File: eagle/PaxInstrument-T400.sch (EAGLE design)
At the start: 133 parts, among them IC1 MCP3424, IC3 SN74LVC1G74DCT, J1 MICRO-SDCARD-CONNECTOR-330006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, Q1 DMP2035U-7, Q2 DMP2035U-7, Q3 DMN2075U-7, Q4 DMN2075U-7, Q5 DMP2035U-7, U1 MCP9800, U2 APX809, U3 MCP73831, U4 MIC5219-3.3V, X1 FH12-12S-1S, Y1 RESONATORSMD

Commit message: Updated SCH and PCB
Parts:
- JP1: value (none) -> ON
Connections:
- removed net DATA1: GND.PF6(ADC6), ICSP1.4, U$3.PF6(ADC6)
- new net RXLED: GND.PB0(SS), U$3.PB0(SS)
- net PWR_ONOFF: now also GND.PF6(ADC6), U$3.PF6(ADC6); no longer GND.PB7, U$3.PB7
- net RTC_INT: now also GND.PB4(ADC11), U$3.PB4(ADC11); no longer GND.PE6, U$3.PE6
- net SW_C: now also GND.PB7, U$3.PB7; no longer GND.PB4(ADC11), U$3.PB4(ADC11)
- net SW_PWR: now also GND.PE6, U$3.PE6; no longer GND.PB0(SS), U$3.PB0(SS)
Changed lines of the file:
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@@
 <part name="GND20" library="SparkFun-Aesthetics" deviceset="GND" device=""/>
 <part name="P+8" library="SparkFun" deviceset="3.3V" device=""/>
-<part name="JP1" library="SparkFun-Passives" deviceset="JUMPER-2" device="SMD-NO">
+<part name="JP1" library="SparkFun-Passives" deviceset="JUMPER-2" device="SMD-NO" value="ON">
 <attribute name="MF" value="N/A"/>
 <attribute name="MPN" value="N/A"/>
@@
 </segment>
 <segment>
-<wire x1="81.28" y1="124.46" x2="83.82" y2="124.46" width="0.1524" layer="91"/>
-<label x="83.82" y="124.46" size="1.778" layer="95"/>
-<pinref part="GND" gate="G$1" pin="PB7"/>
-<pinref part="U$3" gate="G$1" pin="PB7"/>
-<junction x="81.28" y="124.46"/>
+<wire x1="81.28" y1="172.72" x2="83.82" y2="172.72" width="0.1524" layer="91"/>
+<label x="83.82" y="172.72" size="1.778" layer="95"/>
+<pinref part="GND" gate="G$1" pin="PF6(ADC6)"/>
+<pinref part="U$3" gate="G$1" pin="PF6(ADC6)"/>
+<junction x="81.28" y="172.72"/>
 </segment>
 </net>
@@
 </segment>
 <segment>
-<wire x1="81.28" y1="132.08" x2="83.82" y2="132.08" width="0.1524" layer="91"/>
-<label x="83.82" y="132.08" size="1.778" layer="95"/>
-<pinref part="GND" gate="G$1" pin="PB4(ADC11)"/>
-<pinref part="U$3" gate="G$1" pin="PB4(ADC11)"/>
-<junction x="81.28" y="132.08"/>
+<wire x1="81.28" y1="124.46" x2="83.82" y2="124.46" width="0.1524" layer="91"/>
+<label x="83.82" y="124.46" size="1.778" layer="95"/>
+<pinref part="GND" gate="G$1" pin="PB7"/>
+<pinref part="U$3" gate="G$1" pin="PB7"/>
+<junction x="81.28" y="124.46"/>
 </segment>
 </net>
@@
 </segment>
 <segment>
-<wire x1="81.28" y1="116.84" x2="83.82" y2="116.84" width="0.1524" layer="91"/>
-<label x="83.82" y="116.84" size="1.778" layer="95"/>
-<pinref part="GND" gate="G$1" pin="PB0(SS)"/>
-<pinref part="U$3" gate="G$1" pin="PB0(SS)"/>
-<junction x="81.28" y="116.84"/>
+<wire x1="81.28" y1="134.62" x2="83.82" y2="134.62" width="0.1524" layer="91"/>
+<label x="83.82" y="134.62" size="1.778" layer="95"/>
+<pinref part="GND" gate="G$1" pin="PE6"/>
+<pinref part="U$3" gate="G$1" pin="PE6"/>
+<junction x="81.28" y="134.62"/>
 </segment>
 </net>
@@
 </segment>
 <segment>
-<wire x1="81.28" y1="134.62" x2="83.82" y2="134.62" width="0.1524" layer="91"/>
-<label x="83.82" y="134.62" size="1.778" layer="95"/>
-<pinref part="GND" gate="G$1" pin="PE6"/>
-<pinref part="U$3" gate="G$1" pin="PE6"/>
-<junction x="81.28" y="134.62"/>
+<wire x1="81.28" y1="132.08" x2="83.82" y2="132.08" width="0.1524" layer="91"/>
+<label x="83.82" y="132.08" size="1.778" layer="95"/>
+<pinref part="GND" gate="G$1" pin="PB4(ADC11)"/>
+<pinref part="U$3" gate="G$1" pin="PB4(ADC11)"/>
+<junction x="81.28" y="132.08"/>
 </segment>
 </net>
@@
 </segment>
 </net>
-<net name="TXLED" class="0">
-<segment>
-<wire x1="81.28" y1="104.14" x2="83.82" y2="104.14" width="0.1524" layer="91"/>
-<label x="83.82" y="104.14" size="1.778" layer="95"/>
-<pinref part="GND" gate="G$1" pin="PD5"/>
-<pinref part="U$3" gate="G$1" pin="PD5"/>
-<junction x="81.28" y="104.14"/>
-</segment>
-</net>
 <net name="N$10" class="0">
 <segment>
@@
 <pinref part="U$3" gate="G$1" pin="AREF"/>
 <junction x="45.72" y="162.56"/>
-</segment>
-</net>
-<net name="DATA1" class="0">
-<segment>
-<wire x1="81.28" y1="172.72" x2="83.82" y2="172.72" width="0.1524" layer="91"/>
-<label x="83.82" y="172.72" size="1.778" layer="95"/>
-<pinref part="GND" gate="G$1" pin="PF6(ADC6)"/>
-<pinref part="U$3" gate="G$1" pin="PF6(ADC6)"/>
-<junction x="81.28" y="172.72"/>
-</segment>
-<segment>
-<label x="294.64" y="93.98" size="1.778" layer="95"/>
-<pinref part="ICSP1" gate="G$1" pin="4"/>
-<wire x1="294.64" y1="93.98" x2="292.1" y2="93.98" width="0.1524" layer="91"/>
 </segment>
 </net>
@@
 </segment>
 </net>
+<net name="RXLED" class="0">
+<segment>
+<wire x1="81.28" y1="116.84" x2="83.82" y2="116.84" width="0.1524" layer="91"/>
+<label x="83.82" y="116.84" size="1.778" layer="95"/>
+<pinref part="GND" gate="G$1" pin="PB0(SS)"/>
+<pinref part="U$3" gate="G$1" pin="PB0(SS)"/>
+<junction x="81.28" y="116.84"/>
+</segment>
+</net>
+<net name="TXLED" class="0">
+<segment>
+<wire x1="81.28" y1="104.14" x2="83.82" y2="104.14" width="0.1524" layer="91"/>
+<label x="83.82" y="104.14" size="1.778" layer="95"/>
+<pinref part="GND" gate="G$1" pin="PD5"/>
+<pinref part="U$3" gate="G$1" pin="PD5"/>
+<junction x="81.28" y="104.14"/>
+</segment>
+</net>

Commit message: Updated PCB layout
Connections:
- removed net TXLED: GND.PD5, U$3.PD5
- new net DATA1: GND.PF6(ADC6), ICSP1.4, U$3.PF6(ADC6)
- net PWR_ONOFF: now also GND.PD5, U$3.PD5; no longer GND.PF6(ADC6), U$3.PF6(ADC6)
- net RTC_INT: now also GND.PD2(RX), U$3.PD2(RX); no longer GND.PB4(ADC11), U$3.PB4(ADC11)
- net SW_A: now also GND.PE6, U$3.PE6; no longer GND.PD3(TX), U$3.PD3(TX)
- net SW_B: now also GND.PD3(TX), U$3.PD3(TX); no longer GND.PD2(RX), U$3.PD2(RX)
- net SW_C: now also GND.PB4(ADC11), U$3.PB4(ADC11); no longer GND.PB7, U$3.PB7
- net SW_PWR: now also GND.PB7, U$3.PB7; no longer GND.PE6, U$3.PE6
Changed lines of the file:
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@@
 </segment>
 <segment>
-<wire x1="81.28" y1="172.72" x2="83.82" y2="172.72" width="0.1524" layer="91"/>
-<label x="83.82" y="172.72" size="1.778" layer="95"/>
-<pinref part="GND" gate="G$1" pin="PF6(ADC6)"/>
-<pinref part="U$3" gate="G$1" pin="PF6(ADC6)"/>
-<junction x="81.28" y="172.72"/>
+<wire x1="81.28" y1="104.14" x2="83.82" y2="104.14" width="0.1524" layer="91"/>
+<label x="83.82" y="104.14" size="1.778" layer="95"/>
+<pinref part="GND" gate="G$1" pin="PD5"/>
+<pinref part="U$3" gate="G$1" pin="PD5"/>
+<junction x="81.28" y="104.14"/>
 </segment>
 </net>
@@
 </segment>
 <segment>
-<wire x1="81.28" y1="152.4" x2="83.82" y2="152.4" width="0.1524" layer="91"/>
-<label x="83.82" y="152.4" size="1.778" layer="95"/>
-<pinref part="GND" gate="G$1" pin="PD2(RX)"/>
-<pinref part="U$3" gate="G$1" pin="PD2(RX)"/>
-<junction x="81.28" y="152.4"/>
+<wire x1="81.28" y1="149.86" x2="83.82" y2="149.86" width="0.1524" layer="91"/>
+<label x="83.82" y="149.86" size="1.778" layer="95"/>
+<pinref part="GND" gate="G$1" pin="PD3(TX)"/>
+<pinref part="U$3" gate="G$1" pin="PD3(TX)"/>
+<junction x="81.28" y="149.86"/>
 </segment>
 </net>
@@
 </segment>
 <segment>
-<wire x1="81.28" y1="124.46" x2="83.82" y2="124.46" width="0.1524" layer="91"/>
-<label x="83.82" y="124.46" size="1.778" layer="95"/>
-<pinref part="GND" gate="G$1" pin="PB7"/>
-<pinref part="U$3" gate="G$1" pin="PB7"/>
-<junction x="81.28" y="124.46"/>
+<wire x1="81.28" y1="132.08" x2="83.82" y2="132.08" width="0.1524" layer="91"/>
+<label x="83.82" y="132.08" size="1.778" layer="95"/>
+<pinref part="GND" gate="G$1" pin="PB4(ADC11)"/>
+<pinref part="U$3" gate="G$1" pin="PB4(ADC11)"/>
+<junction x="81.28" y="132.08"/>
 </segment>
 </net>
@@
 </segment>
 <segment>
-<wire x1="81.28" y1="149.86" x2="83.82" y2="149.86" width="0.1524" layer="91"/>
-<label x="83.82" y="149.86" size="1.778" layer="95"/>
-<pinref part="GND" gate="G$1" pin="PD3(TX)"/>
-<pinref part="U$3" gate="G$1" pin="PD3(TX)"/>
-<junction x="81.28" y="149.86"/>
+<wire x1="81.28" y1="134.62" x2="83.82" y2="134.62" width="0.1524" layer="91"/>
+<label x="83.82" y="134.62" size="1.778" layer="95"/>
+<pinref part="GND" gate="G$1" pin="PE6"/>
+<pinref part="U$3" gate="G$1" pin="PE6"/>
+<junction x="81.28" y="134.62"/>
 </segment>
 </net>
@@
 </segment>
 <segment>
-<wire x1="81.28" y1="134.62" x2="83.82" y2="134.62" width="0.1524" layer="91"/>
-<label x="83.82" y="134.62" size="1.778" layer="95"/>
-<pinref part="GND" gate="G$1" pin="PE6"/>
-<pinref part="U$3" gate="G$1" pin="PE6"/>
-<junction x="81.28" y="134.62"/>
+<wire x1="81.28" y1="124.46" x2="83.82" y2="124.46" width="0.1524" layer="91"/>
+<label x="83.82" y="124.46" size="1.778" layer="95"/>
+<pinref part="GND" gate="G$1" pin="PB7"/>
+<pinref part="U$3" gate="G$1" pin="PB7"/>
+<junction x="81.28" y="124.46"/>
 </segment>
 </net>
@@
 </segment>
 <segment>
-<wire x1="81.28" y1="132.08" x2="83.82" y2="132.08" width="0.1524" layer="91"/>
-<label x="83.82" y="132.08" size="1.778" layer="95"/>
-<pinref part="GND" gate="G$1" pin="PB4(ADC11)"/>
-<pinref part="U$3" gate="G$1" pin="PB4(ADC11)"/>
-<junction x="81.28" y="132.08"/>
+<wire x1="81.28" y1="152.4" x2="83.82" y2="152.4" width="0.1524" layer="91"/>
+<label x="83.82" y="152.4" size="1.778" layer="95"/>
+<pinref part="GND" gate="G$1" pin="PD2(RX)"/>
+<pinref part="U$3" gate="G$1" pin="PD2(RX)"/>
+<junction x="81.28" y="152.4"/>
 </segment>
 </net>
@@
 </segment>
 </net>
-<net name="TXLED" class="0">
-<segment>
-<wire x1="81.28" y1="104.14" x2="83.82" y2="104.14" width="0.1524" layer="91"/>
-<label x="83.82" y="104.14" size="1.778" layer="95"/>
-<pinref part="GND" gate="G$1" pin="PD5"/>
-<pinref part="U$3" gate="G$1" pin="PD5"/>
-<junction x="81.28" y="104.14"/>
-</segment>
-</net>
+<net name="DATA1" class="0">
+<segment>
+<wire x1="81.28" y1="172.72" x2="83.82" y2="172.72" width="0.1524" layer="91"/>
+<label x="83.82" y="172.72" size="1.778" layer="95"/>
+<pinref part="GND" gate="G$1" pin="PF6(ADC6)"/>
+<pinref part="U$3" gate="G$1" pin="PF6(ADC6)"/>
+<junction x="81.28" y="172.72"/>
+</segment>
+<segment>
+<pinref part="ICSP1" gate="G$1" pin="4"/>
+<wire x1="292.1" y1="93.98" x2="294.64" y2="93.98" width="0.1524" layer="91"/>
+<label x="294.64" y="93.98" size="1.778" layer="95"/>
+</segment>
+</net>

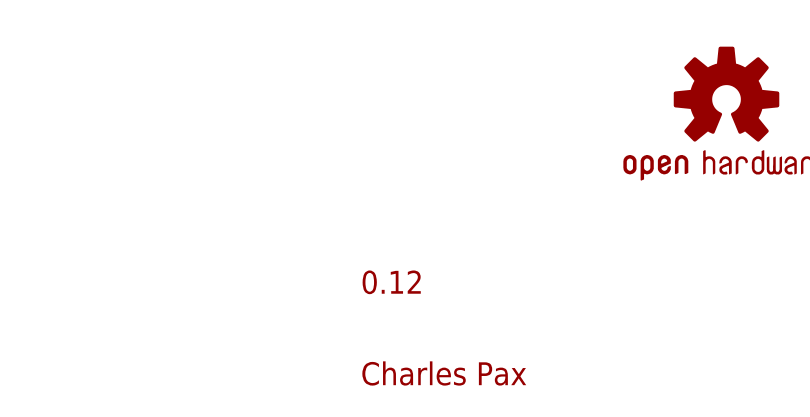
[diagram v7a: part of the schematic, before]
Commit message: Updated Schematic
updated version number on schematic
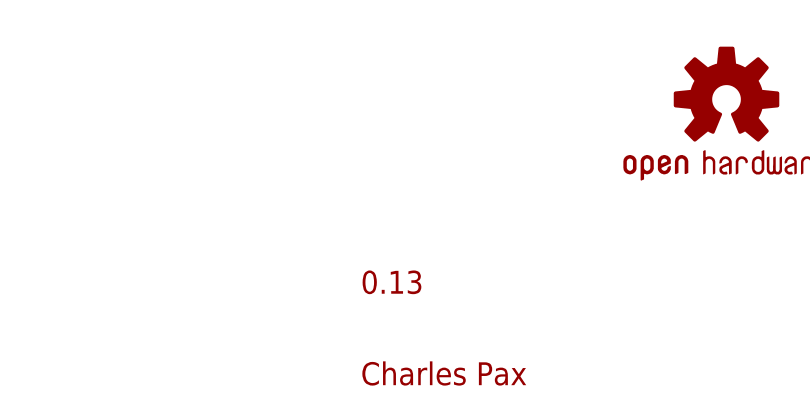
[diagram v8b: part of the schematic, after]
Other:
- note added: "0.13"
- note removed: "0.12"
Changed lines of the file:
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@@
 <wire x1="195.58" y1="154.94" x2="195.58" y2="193.04" width="0.2032" layer="94"/>
 <text x="198.12" y="187.96" size="3.81" layer="94">Temp sensor</text>
-<text x="330.2" y="15.24" size="2.54" layer="94" align="center-left">0.12</text>
+<text x="330.2" y="15.24" size="2.54" layer="94" align="center-left">0.13</text>
 <wire x1="256.54" y1="73.66" x2="314.96" y2="73.66" width="0.2032" layer="94"/>
 <wire x1="256.54" y1="111.76" x2="256.54" y2="73.66" width="0.2032" layer="94"/>
